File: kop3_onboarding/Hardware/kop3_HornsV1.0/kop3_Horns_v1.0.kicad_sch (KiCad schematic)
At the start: 0 parts

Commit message: Horn Breakout Board Schematic
Created the Horn Breakout Board Schematic following the wiki steps. This includes decoupling capacitors, half of an rc filter, and two horns in series.
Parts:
- added C1: 100 uF, symbol device:C_Polarized_Small_US
- added C10: C, symbol device:C
- added C11, C12, C2: .01 uF, symbol device:C
- added C4, C5: 10 uF, symbol device:C
- added C6, C7: 1 uF, symbol device:C
- added D2: S2JTR, Diode_SMD:D_SMB, symbol Diode:S2JTR
- added F1: 2A, symbol device:Fuse
- added J1: Power, symbol Connector_Generic:Conn_01x03
- added J2: HORN_CONTROL, symbol Connector_Generic:Conn_01x02
- added J3: HORN_OUT1, symbol Connector_Generic:Conn_01x02
- added J4: HORN_OUT2, symbol Connector_Generic:Conn_01x02
- added Q1: IRF540N, Package_TO_SOT_THT:TO-220-3_Vertical, symbol Transistor_FET:IRF540N
- added R1: 1K, symbol Device:R_Small_US
- added SW1: SW_Push, symbol Switch:SW_Push
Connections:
- new net: F1.1, J4.2 (Pin_2)
- new net: D2.2 (A), F1.2
- new net: D2.1 (K), Q1.2 (D), SW1.1
- new net: J3.2 (Pin_2), J4.1 (Pin_1)
- new net: C10.1, R1.1
- new net +24V: C1.1, C11.1, C12.1, C2.1, C4.1, C5.1, C6.1, C7.1, J1.2 (Pin_2), J3.1 (Pin_1)
- new net GND: C1.2, C10.2, C11.2, C12.2, C2.2, C4.2, C5.2, C6.2, C7.2, J1.1 (Pin_1), J1.3 (Pin_3), J2.1 (Pin_1), Q1.3 (S), SW1.2
- new net HORN_CONTROL: J2.2 (Pin_2), Q1.1 (G), R1.2
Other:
- note added: "Decoupling Capacitors"
- note added: "Horn Control"
- note added: "Horn Out"
- note added: "Power Supply"
- title: Template -> Horn Breakout Board Project

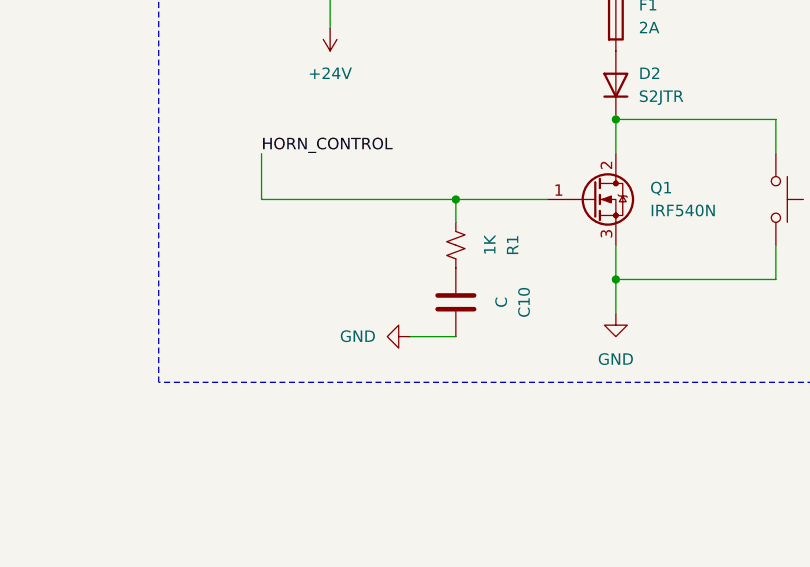
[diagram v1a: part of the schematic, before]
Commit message: PCB Layout for Horn Breakout Board Done.
Created the PCB for the Horn Breakout Board.
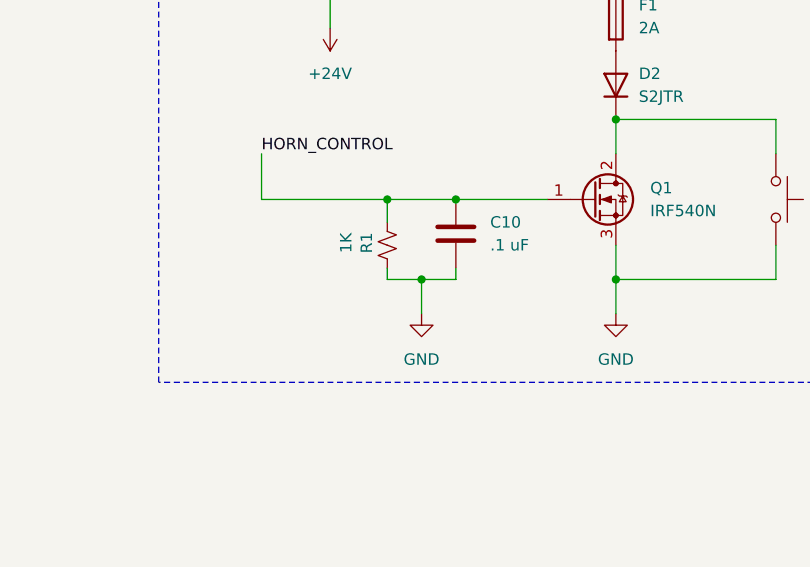
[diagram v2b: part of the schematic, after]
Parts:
- C1, C11, C12, C2, C4, C5, C6, C7: footprint (none) -> Capacitor_SMD:C_0805_2012Metric_Pad1.18x1.45mm_HandSolder
- C10: value C -> .1 uF; footprint (none) -> Capacitor_SMD:C_0805_2012Metric_Pad1.18x1.45mm_HandSolder
- F1: footprint (none) -> Fuse:Fuse_0805_2012Metric_Pad1.15x1.40mm_HandSolder
- J1: footprint (none) -> Connector_Molex:Molex_KK-254_AE-6410-03A_1x03_P2.54mm_Vertical
- J2, J3, J4: footprint (none) -> Connector_Molex:Molex_KK-254_AE-6410-02A_1x02_P2.54mm_Vertical
- R1: footprint (none) -> Resistor_THT:R_Axial_DIN0204_L3.6mm_D1.6mm_P5.08mm_Horizontal
- SW1: footprint (none) -> Button_Switch_SMD:SW_Push_1P1T_NO_6x6mm_H9.5mm
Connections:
- net GND: now also R1.1
- net HORN_CONTROL: now also C10.1
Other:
- moved on the sheet: C10, R1
